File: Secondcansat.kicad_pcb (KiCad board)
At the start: 2 copper layers, 74 x 74 mm, 65 parts, among them IC1 XBP9B-XCWT-001, J1 OpenlogBreakout, J10 SDA, J11 5V, J12 Tx, J13 Rx, J14 Battery_Holder_keystone 1079, J2 camerapower, J3 Pressure_MS5607, J4 Debugger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

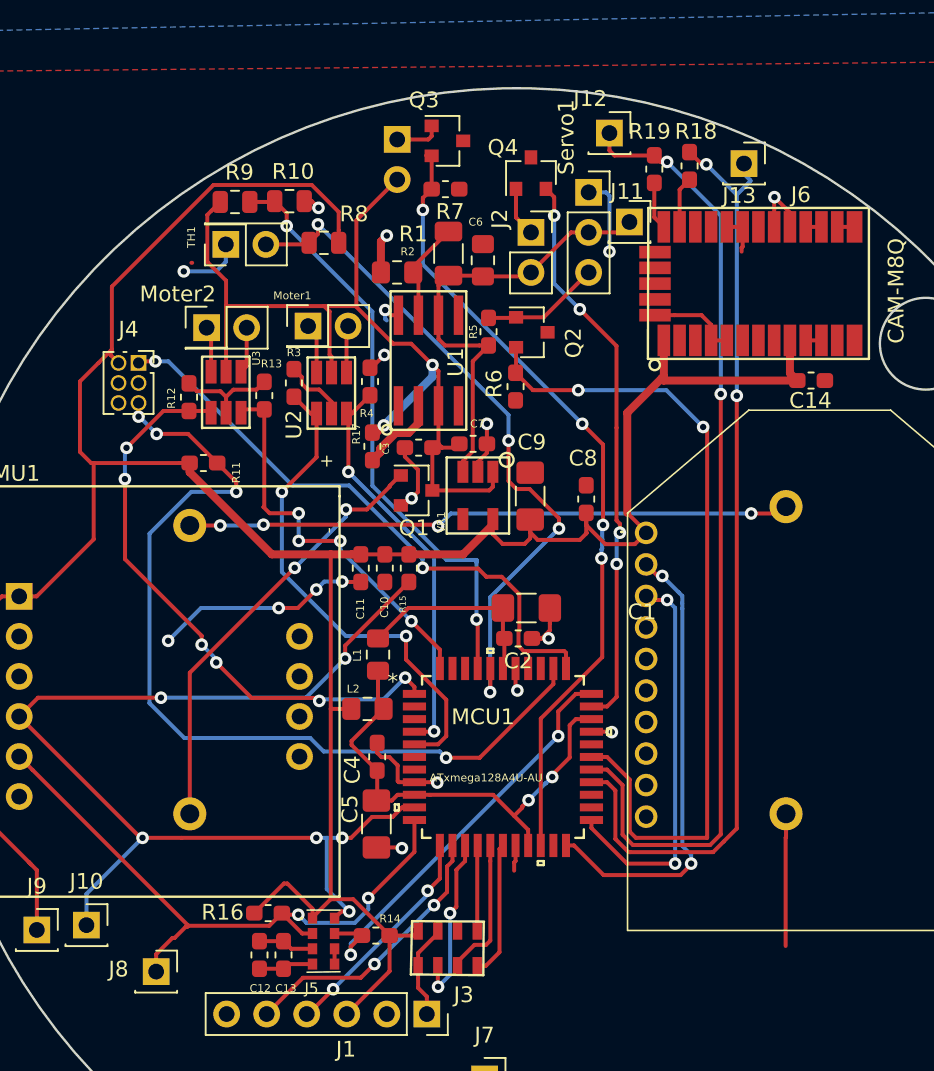
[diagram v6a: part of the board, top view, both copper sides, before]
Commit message: added pull down resistors
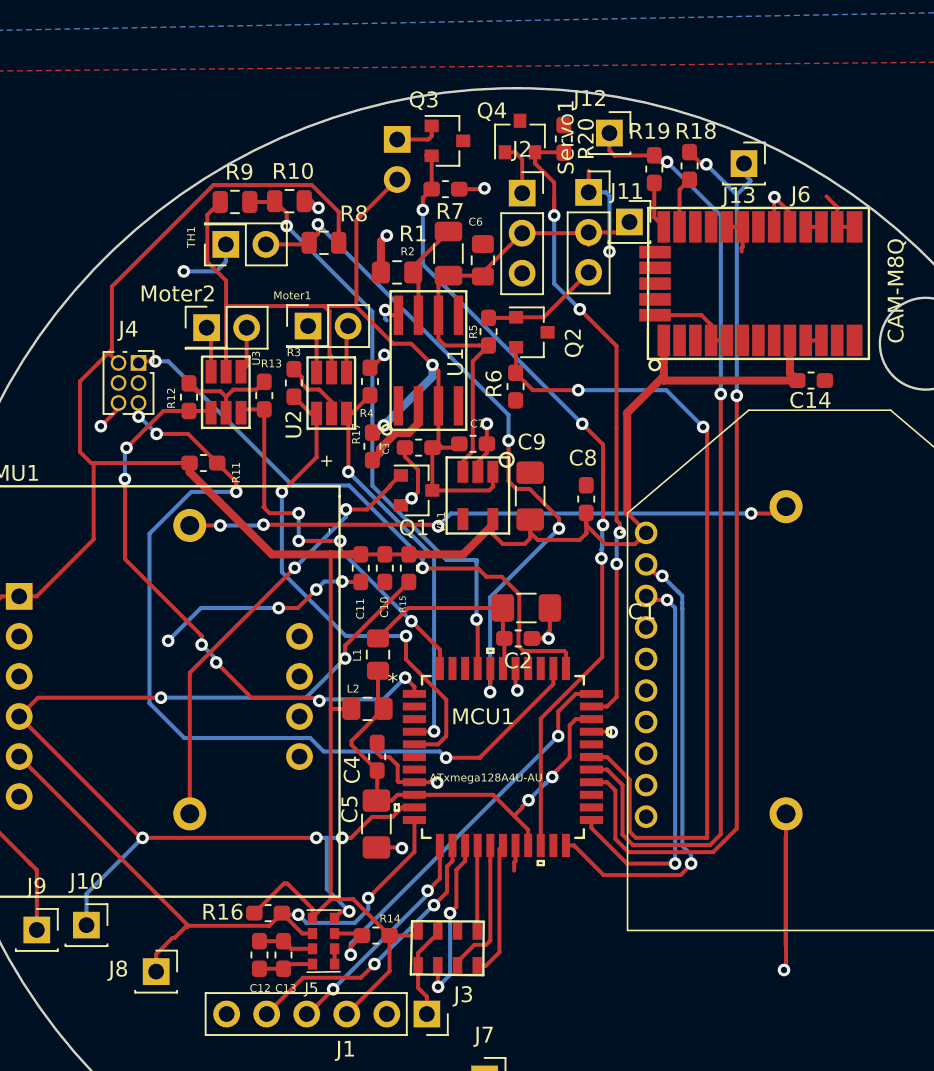
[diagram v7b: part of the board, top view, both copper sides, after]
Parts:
- added R20: 10kohm, Resistor_SMD:R_0603_1608Metric_Pad1.05x0.95mm_HandSolder, F.Cu at (89.6, 64.9)
- J2: value camerapower -> Camera; footprint Connector_PinSocket_2.54mm:PinSocket_1x02_P2.54mm_Vertical -> Connector_PinSocket_2.54mm:PinSocket_1x03_P2.54mm_Vertical
- moved J2 2.55 mm to (87.0, 68.3)
- moved Q4 2.42 mm to (86.8, 64.7)
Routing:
- net GND: track 92.6 -> 109.7 mm, vias 18 -> 21
- net cameraon: track 36.1 -> 41.5 mm
- net +5V: track 29.2 -> 30.2 mm

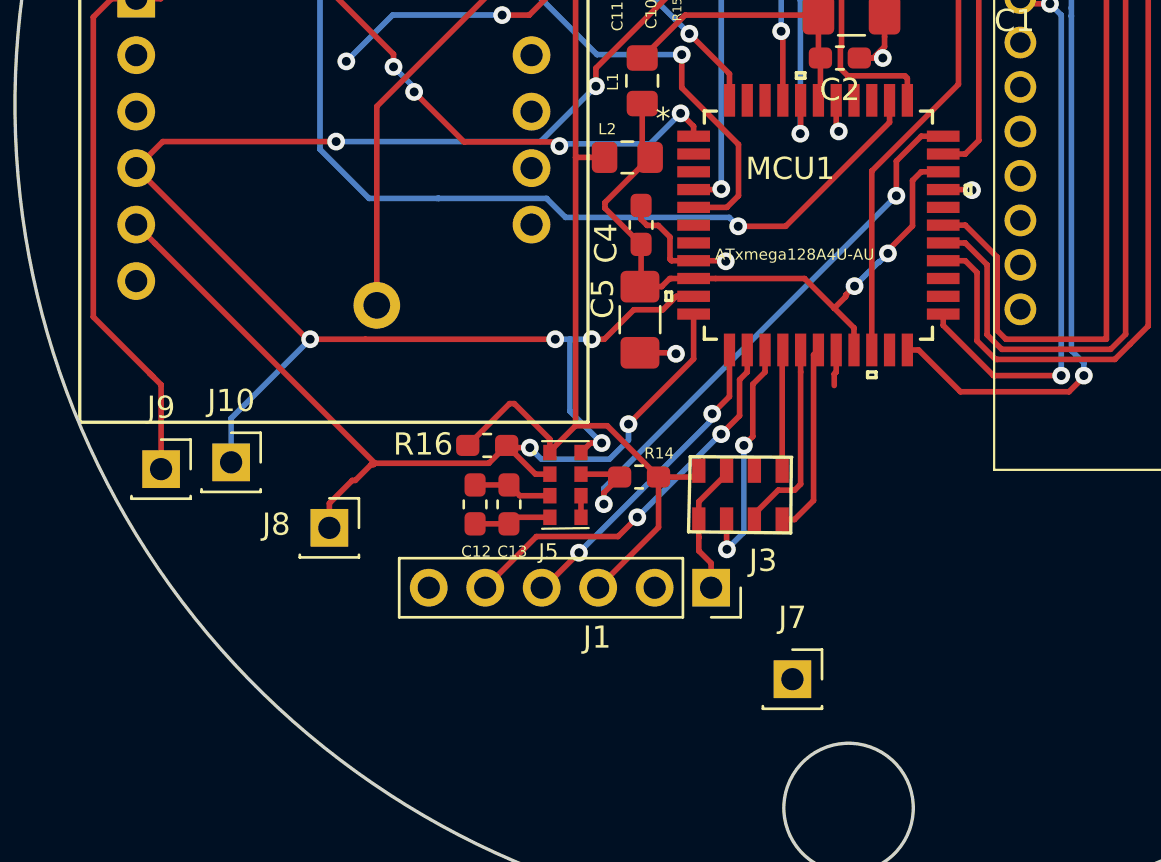
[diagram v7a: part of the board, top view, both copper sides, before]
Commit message: changed footprint for Osram
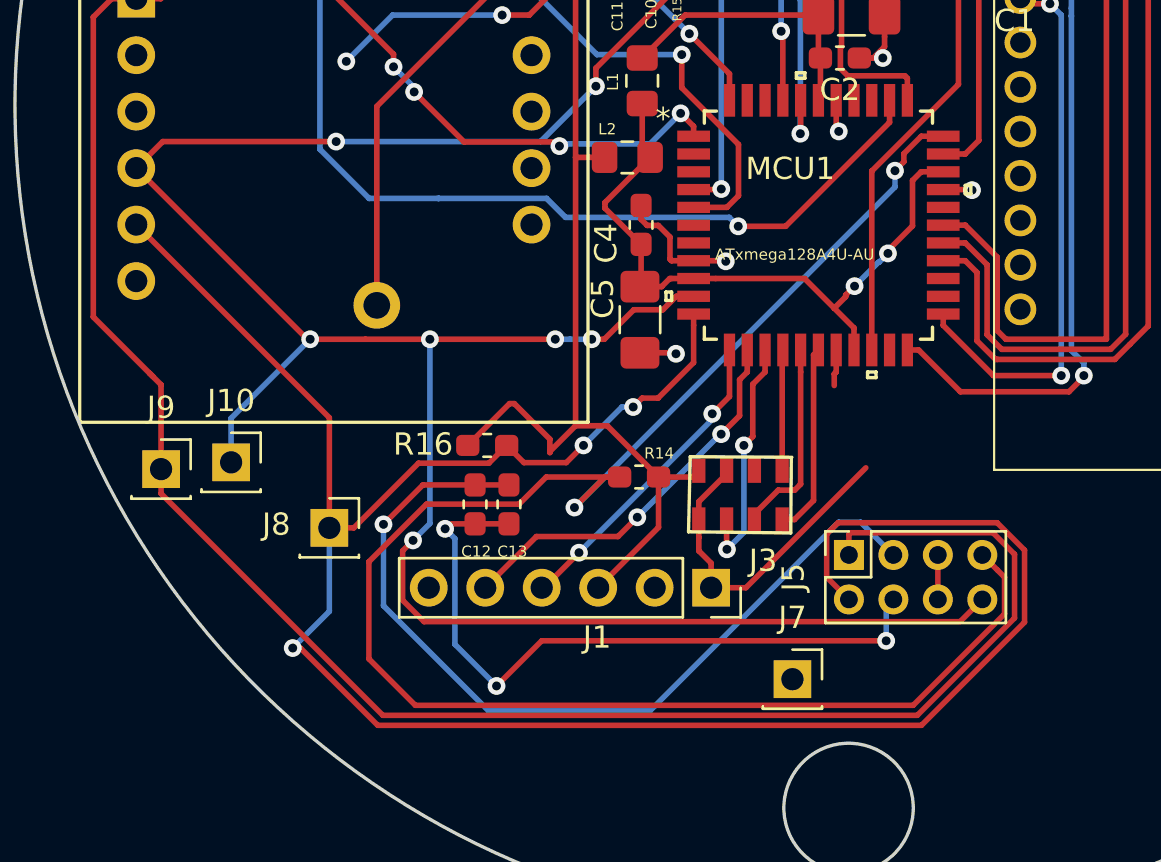
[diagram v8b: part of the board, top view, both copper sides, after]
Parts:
- J5: footprint CanSAT2ndtry:SFH7776 -> Connector_PinSocket_2.00mm:PinSocket_2x04_P2.00mm_Vertical
- moved J5 13.1 mm to (87.1, 118.9)
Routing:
- net SCL: track 40.8 -> 98.1 mm, vias 2 -> 3
- net +3V3: track 182.4 -> 239.5 mm
- net INT: track 26.8 -> 78.2 mm
- net Net-(C12-Pad2): track 3.56 -> 39.1 mm, vias 0 -> 1
- net SDA: track 71.2 -> 103.9 mm, vias 6 -> 7
- net Net-(C12-Pad1): track 3.49 -> 31.4 mm, vias 0 -> 3
- net GND: track 109.7 -> 118.9 mm
- net Net-(J5-Pad5): track 0.97 -> 2.00 mm
